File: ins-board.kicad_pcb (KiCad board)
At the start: 4 copper layers, 50 x 23 mm, 94 parts, among them P1 POWER, P2 Power (Solder Pad), Q1 FDN306P, Q2 FDC638APZ, U1 24LC128, U10 HMC5883L, U11 H3LIS331DL, U2 STM32F415RGT6, U3 LTC4412, U4 MAX3051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

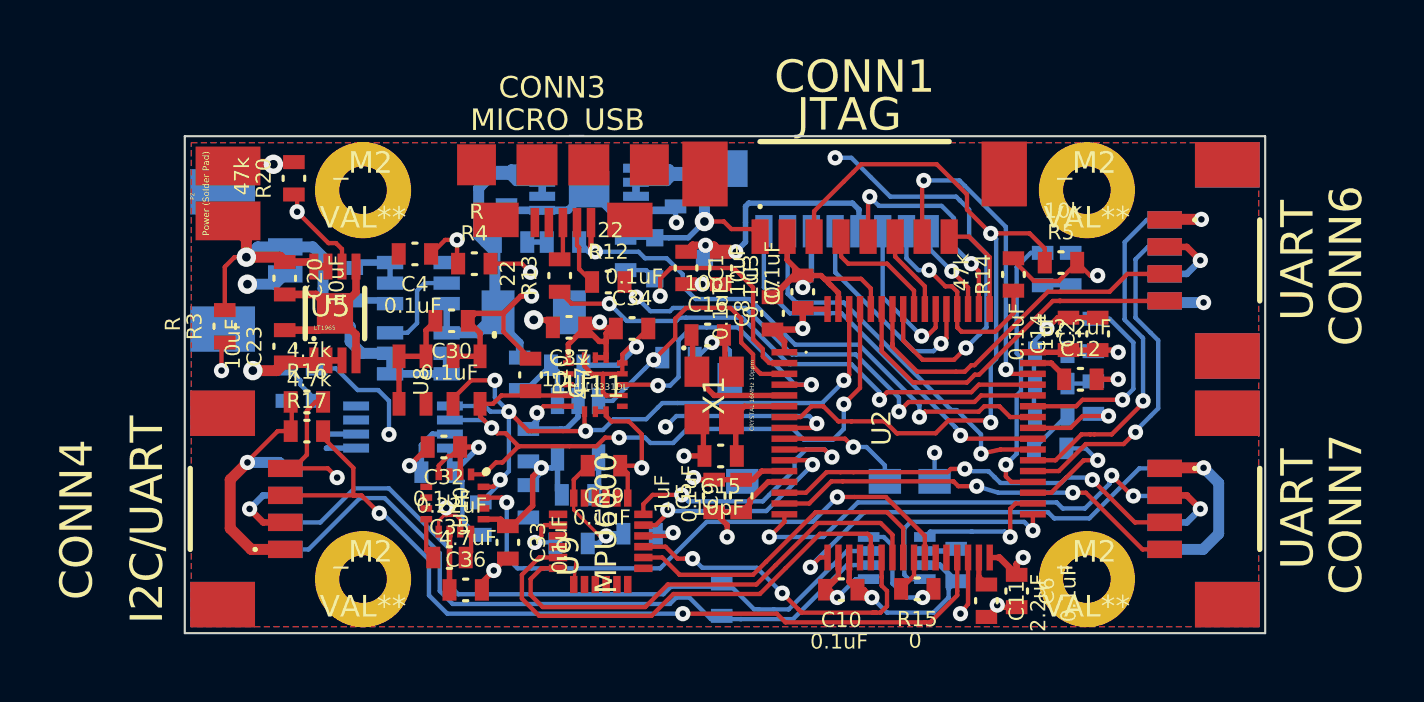
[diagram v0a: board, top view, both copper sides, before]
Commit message: connect molex mechanical connector pads to GND
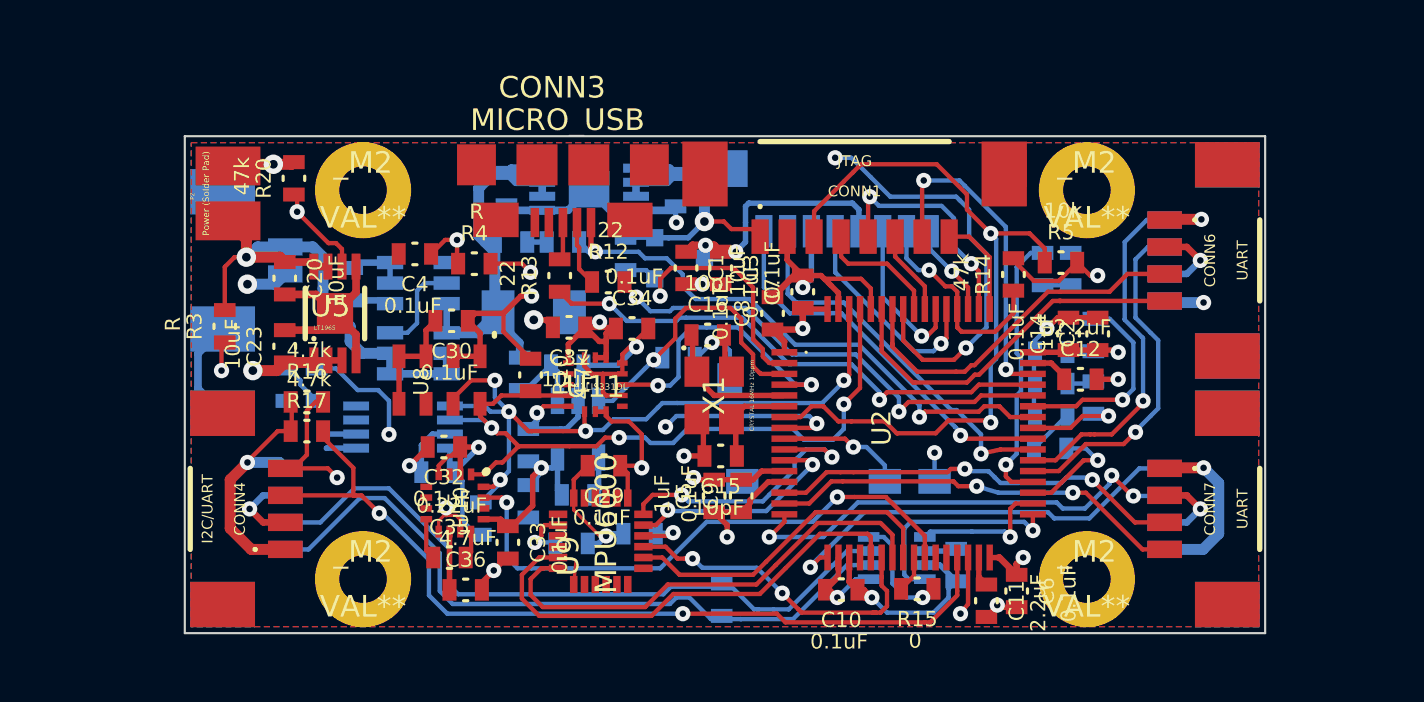
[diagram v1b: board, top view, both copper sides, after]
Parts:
- P1: value POWER -> PWR
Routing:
- net GND: track 133.2 -> 138.2 mm

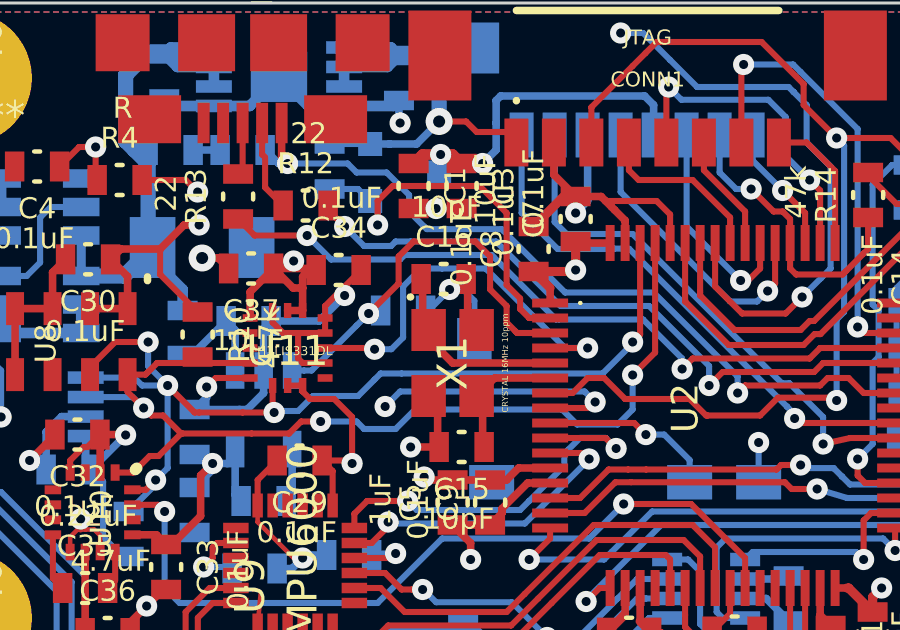
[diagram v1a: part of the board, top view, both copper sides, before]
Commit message: keepout zones for sd card holder in gnd-fill
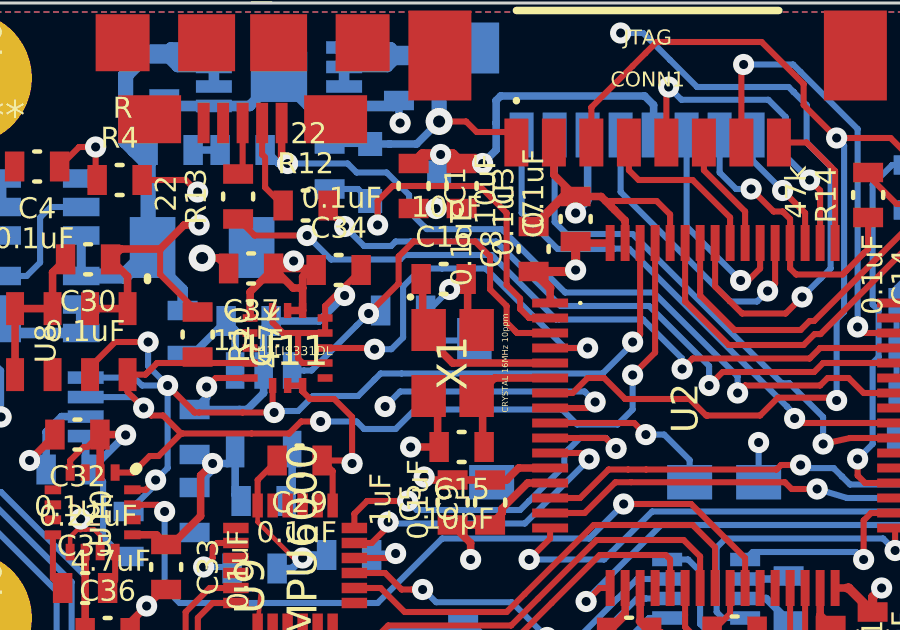
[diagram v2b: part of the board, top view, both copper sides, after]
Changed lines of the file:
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@@
   (page A3)
   (layers
-    (15 F.Cu signal)
-    (2 Inner2.Cu mixed)
-    (1 "Inner1.Cu(GND)" power)
+    (15 F.Cu signal hide)
+    (2 Inner2.Cu mixed hide)
+    (1 "Inner1.Cu(GND)" power hide)
     (0 B.Cu signal)
     (16 B.Adhes user)
@@
   )
   (setup
-    (last_trace_width 0.254)
+    (last_trace_width 0.2032)
     (user_trace_width 0.1524)
     (user_trace_width 0.2032)
@@
   (segment (start 66.25 38.75) (end 66 39) (width 0.2032) (layer F.Cu) (net 51))
   (segment (start 66.25 38.75) (end 66 39) (width 0.2032) (layer F.Cu) (net 51))
+  (segment (start 57.225 37.25) (end 55.78 37.25) (width 0.2032) (layer B.Cu) (net 52) (status 400000))
+  (segment (start 55.6 37.07) (end 55.6 36.25) (width 0.2032) (layer B.Cu) (net 52) (status 800000))
+  (segment (start 55.78 37.25) (end 55.6 37.07) (width 0.2032) (layer B.Cu) (net 52))
   (segment (start 33.75 38.825) (end 32.61 37.685) (width 0.3556) (layer B.Cu) (net 52))
   (segment (start 32.61 36.065) (end 33.75 34.925) (width 0.3556) (layer B.Cu) (net 52))
@@
   (segment (start 44.1 43.55) (end 44.1 43.2) (width 0.2032) (layer F.Cu) (net 52))
   (via (at 44.1 43.2) (size 0.706) (layers F.Cu B.Cu) (net 52))
-  (segment (start 57.225 37.25) (end 57.225 35.925) (width 0.2032) (layer B.Cu) (net 52))
-  (segment (start 56.85 35.55) (end 56.4 35.55) (width 0.2032) (layer B.Cu) (net 52))
-  (segment (start 57.225 35.925) (end 56.85 35.55) (width 0.2032) (layer B.Cu) (net 52))
   (segment (start 46.15 31.9) (end 47.6 31.9) (width 0.2032) (layer F.Cu) (net 52))
   (via (at 48 32.3) (size 0.706) (layers F.Cu B.Cu) (net 52))
@@
       )
     )
+  )
+  (zone (net 0) (net_name "") (layer B.Cu) (hatch edge 0.508)
+    (connect_pads (clearance 0.254))
+    (min_thickness 0.254)
+    (keepout (tracks not_allowed) (vias not_allowed) (copperpour not_allowed))
+    (fill (arc_segments 16) (thermal_gap 0.508) (thermal_bridge_width 0.508))
+    (polygon
+      (pts
+        (xy 56.85 35.11) (xy 56.85 36.39) (xy 57.76 36.39) (xy 57.76 35.21) (xy 57.65 35.11)
+      )
+    )
+  )
+  (zone (net 0) (net_name "") (layer B.Cu) (hatch edge 0.508)
+    (connect_pads (clearance 0.254))
+    (min_thickness 0.254)
+    (keepout (tracks not_allowed) (vias not_allowed) (copperpour not_allowed))
+    (fill (arc_segments 16) (thermal_gap 0.508) (thermal_bridge_width 0.508))
+    (polygon
+      (pts
+        (xy 56.32 39.68) (xy 56.32 41.33) (xy 59.92 41.33) (xy 59.93 39.68)
+      )
+    )
+  )
+  (zone (net 0) (net_name "") (layer B.Cu) (hatch edge 0.508)
+    (connect_pads (clearance 0.254))
+    (min_thickness 0.254)
+    (keepout (tracks not_allowed) (vias not_allowed) (copperpour not_allowed))
+    (fill (arc_segments 16) (thermal_gap 0.508) (thermal_bridge_width 0.508))
+    (polygon
+      (pts
+        (xy 62.27 41.45) (xy 62.27 42.22) (xy 63.59 42.22) (xy 63.59 41.45)
+      )
+    )

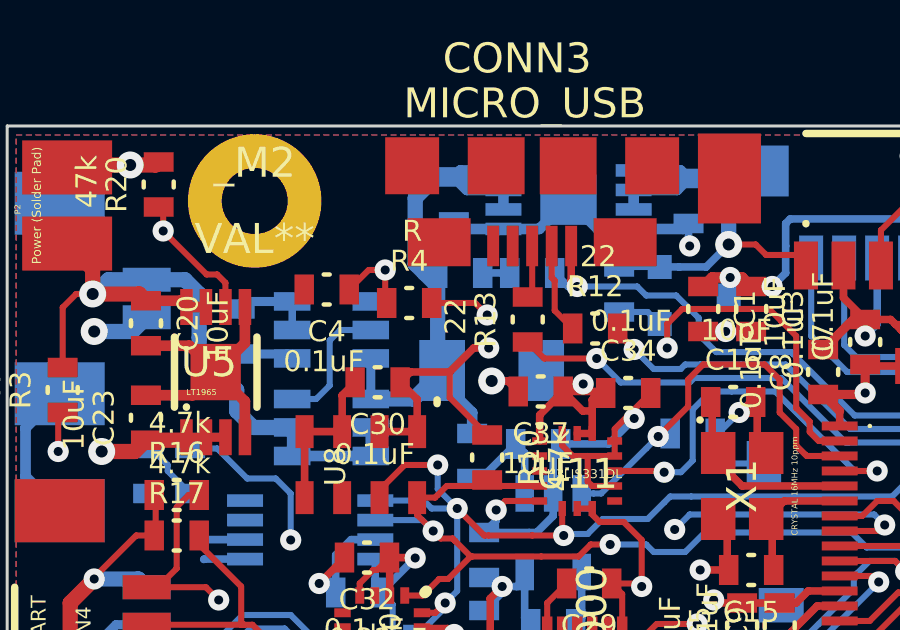
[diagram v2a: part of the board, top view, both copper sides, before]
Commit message: add V_USB diode with correct footprint
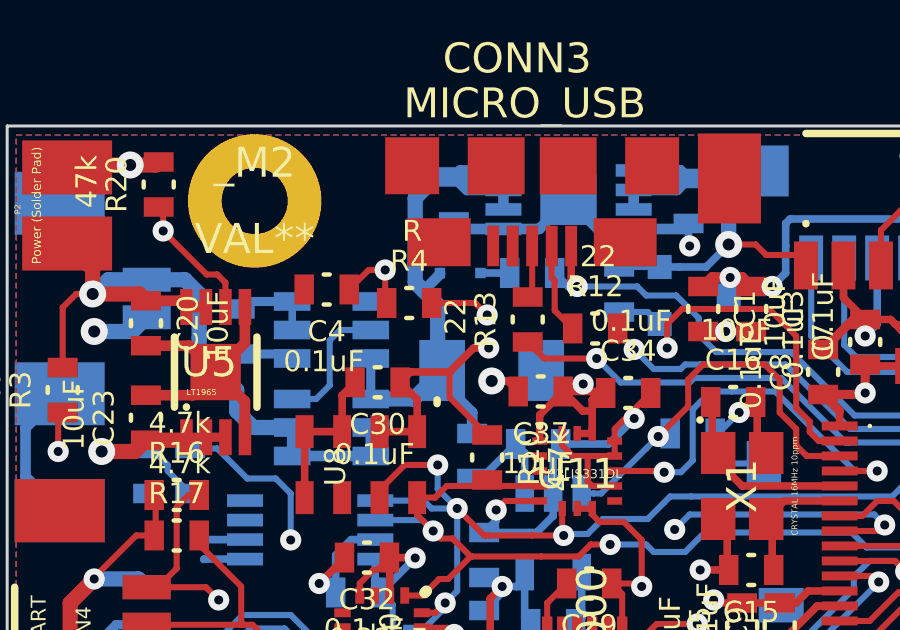
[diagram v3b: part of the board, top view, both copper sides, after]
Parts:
- D6: value DIODESCH -> BAS52-02V; footprint _0603-W -> _SC79
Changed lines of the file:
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@@
     (thickness 1.6)
     (drawings 13)
-    (tracks 1261)
+    (tracks 1263)
     (zones 0)
     (modules 94)
@@
   )
   (setup
-    (last_trace_width 0.2032)
+    (last_trace_width 0.3556)
     (user_trace_width 0.1524)
     (user_trace_width 0.2032)
@@
     (mod_text_size 1 1)
     (mod_text_width 0.15)
-    (pad_size 1.8 3)
+    (pad_size 0.35 0.35)
     (pad_drill 0)
     (pad_to_mask_clearance 0)
@@
     )
   )
-  (module _0603-W (layer B.Cu)
-    (at 47.1 30.9 180)
-    (fp_text reference D6 (at 0 1.4 180) (layer B.SilkS)
-      (effects (font (size 0.7 0.7) (thickness 0.15)) (justify mirror))
-    )
-    (fp_text value DIODESCH (at 0.1 2.4 180) (layer B.SilkS)
-      (effects (font (size 0.7 0.7) (thickness 0.15)) (justify mirror))
-    )
-    (fp_line (start 0.1 -0.5) (end -0.1 -0.5) (layer B.SilkS) (width 0.15))
-    (fp_line (start 0.1 0.5) (end -0.1 0.5) (layer B.SilkS) (width 0.15))
-    (pad 2 smd rect (at 0.75 0 180) (size 0.65 1)
-      (layers B.Cu B.Paste B.Mask)
-      (net 50 /V_IN)
-    )
-    (pad 1 smd rect (at -0.75 0 180) (size 0.65 1)
-      (layers B.Cu B.Paste B.Mask)
-      (net 53 N-000001)
-    )
-  )
   (module _MPU-60X0 (layer F.Cu)
     (at 51.25 44.75 90)
@@
     )
   )
+  (module _SC79 (layer B.Cu)
+    (at 47.1 30.9 180)
+    (fp_text reference D6 (at 0 0 180) (layer B.SilkS)
+      (effects (font (size 0.5 0.5) (thickness 0.125)) (justify mirror))
+    )
+    (fp_text value BAS52-02V (at 0 0 180) (layer B.SilkS)
+      (effects (font (size 0.5 0.5) (thickness 0.125)) (justify mirror))
+    )
+    (fp_line (start 0.254 0.254) (end 0.254 -0.254) (layer B.SilkS) (width 0.15))
+    (fp_line (start 0.1 -0.5) (end -0.1 -0.5) (layer B.SilkS) (width 0.15))
+    (fp_line (start 0.1 0.5) (end -0.1 0.5) (layer B.SilkS) (width 0.15))
+    (pad 2 smd rect (at 0.675 0 180) (size 0.35 0.35)
+      (layers B.Cu B.Paste B.Mask)
+      (net 50 /V_IN)
+    )
+    (pad 1 smd rect (at -0.675 0 180) (size 0.35 0.35)
+      (layers B.Cu B.Paste B.Mask)
+      (net 53 N-000001)
+    )
+  )
   (dimension 50 (width 0.3) (layer Dwgs.User)
     (gr_text "50.000 mm" (at 57 20.900001) (layer Dwgs.User)
@@
   (segment (start 39.75 33.6) (end 41.35 33.6) (width 0.3048) (layer B.Cu) (net 49))
   (segment (start 41.35 33.6) (end 41.5 33.75) (width 0.3048) (layer B.Cu) (net 49))
-  (segment (start 46.35 30.9) (end 45.9 30.9) (width 0.254) (layer B.Cu) (net 50))
+  (segment (start 46.425 30.9) (end 46.425 30.945) (width 0.3556) (layer B.Cu) (net 50) (status C00000))
+  (segment (start 46.425 30.945) (end 45.88 31.49) (width 0.3556) (layer B.Cu) (net 50) (status 400000))
+  (segment (start 46.35 31.96) (end 45.88 31.49) (width 0.508) (layer B.Cu) (net 50))
+  (segment (start 45.88 31.49) (end 45.6 31.21) (width 0.508) (layer B.Cu) (net 50))
+  (segment (start 45.6 31.21) (end 45.6 30.6) (width 0.508) (layer B.Cu) (net 50))
   (segment (start 47.5 36.25) (end 47.5 35.55) (width 0.3556) (layer B.Cu) (net 50))
   (segment (start 46.499 34.549) (end 46.499 34.15) (width 0.3556) (layer B.Cu) (net 50))
@@
   (segment (start 45.549 35.1) (end 46.499 34.15) (width 0.508) (layer B.Cu) (net 50))
   (segment (start 46.8884 27.698) (end 46.302 27.698) (width 0.508) (layer B.Cu) (net 50))
-  (segment (start 45.6 30.6) (end 45.9 30.9) (width 0.508) (layer B.Cu) (net 50))
-  (segment (start 45.9 30.9) (end 46.35 31.35) (width 0.508) (layer B.Cu) (net 50))
-  (segment (start 45.6 28.4) (end 45.6 30.6) (width 0.508) (layer B.Cu) (net 50))
   (segment (start 46.302 27.698) (end 45.6 28.4) (width 0.508) (layer B.Cu) (net 50))
-  (segment (start 46.35 31.35) (end 46.35 34.001) (width 0.508) (layer B.Cu) (net 50))
+  (segment (start 45.6 28.4) (end 45.6 30.6) (width 0.508) (layer B.Cu) (net 50))
+  (segment (start 46.35 31.96) (end 46.35 34.001) (width 0.508) (layer B.Cu) (net 50))
   (segment (start 46.35 34.001) (end 46.499 34.15) (width 0.508) (layer B.Cu) (net 50))
   (segment (start 48.5418 28.1328) (end 47.3232 28.1328) (width 0.3556) (layer B.Cu) (net 50))
@@
   (segment (start 66.25 38.75) (end 66 39) (width 0.2032) (layer F.Cu) (net 51))
   (segment (start 66.25 38.75) (end 66 39) (width 0.2032) (layer F.Cu) (net 51))
-  (segment (start 57.225 37.25) (end 55.78 37.25) (width 0.2032) (layer B.Cu) (net 52) (status 400000))
-  (segment (start 55.6 37.07) (end 55.6 36.25) (width 0.2032) (layer B.Cu) (net 52) (status 800000))
+  (segment (start 57.225 37.25) (end 55.78 37.25) (width 0.2032) (layer B.Cu) (net 52))
+  (segment (start 55.6 37.07) (end 55.6 36.25) (width 0.2032) (layer B.Cu) (net 52))
   (segment (start 55.78 37.25) (end 55.6 37.07) (width 0.2032) (layer B.Cu) (net 52))
   (segment (start 33.75 38.825) (end 32.61 37.685) (width 0.3556) (layer B.Cu) (net 52))

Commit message: optimize routing
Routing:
- net GND: track 138.4 -> 140.3 mm, vias 24 -> 25
- net /Sensors/I2C_SDA: track 33.9 -> 34.7 mm
- net /V_BAT_MON_AD: track 56.4 -> 56.9 mm
